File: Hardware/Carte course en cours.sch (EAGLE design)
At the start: 41 parts, among them J2 AVR_SPI_PROG_3X2NS, J3 PWR IN, J4 RC receiver, J5 ESC, J6 ESC, J7 MICRO-SD_CARD_SOCKET, J8 ESC, U1 LM317, U2 ATMEGA328P_TQFP, U3 FT232RL, U4 MPU6050, Y1 8MHz

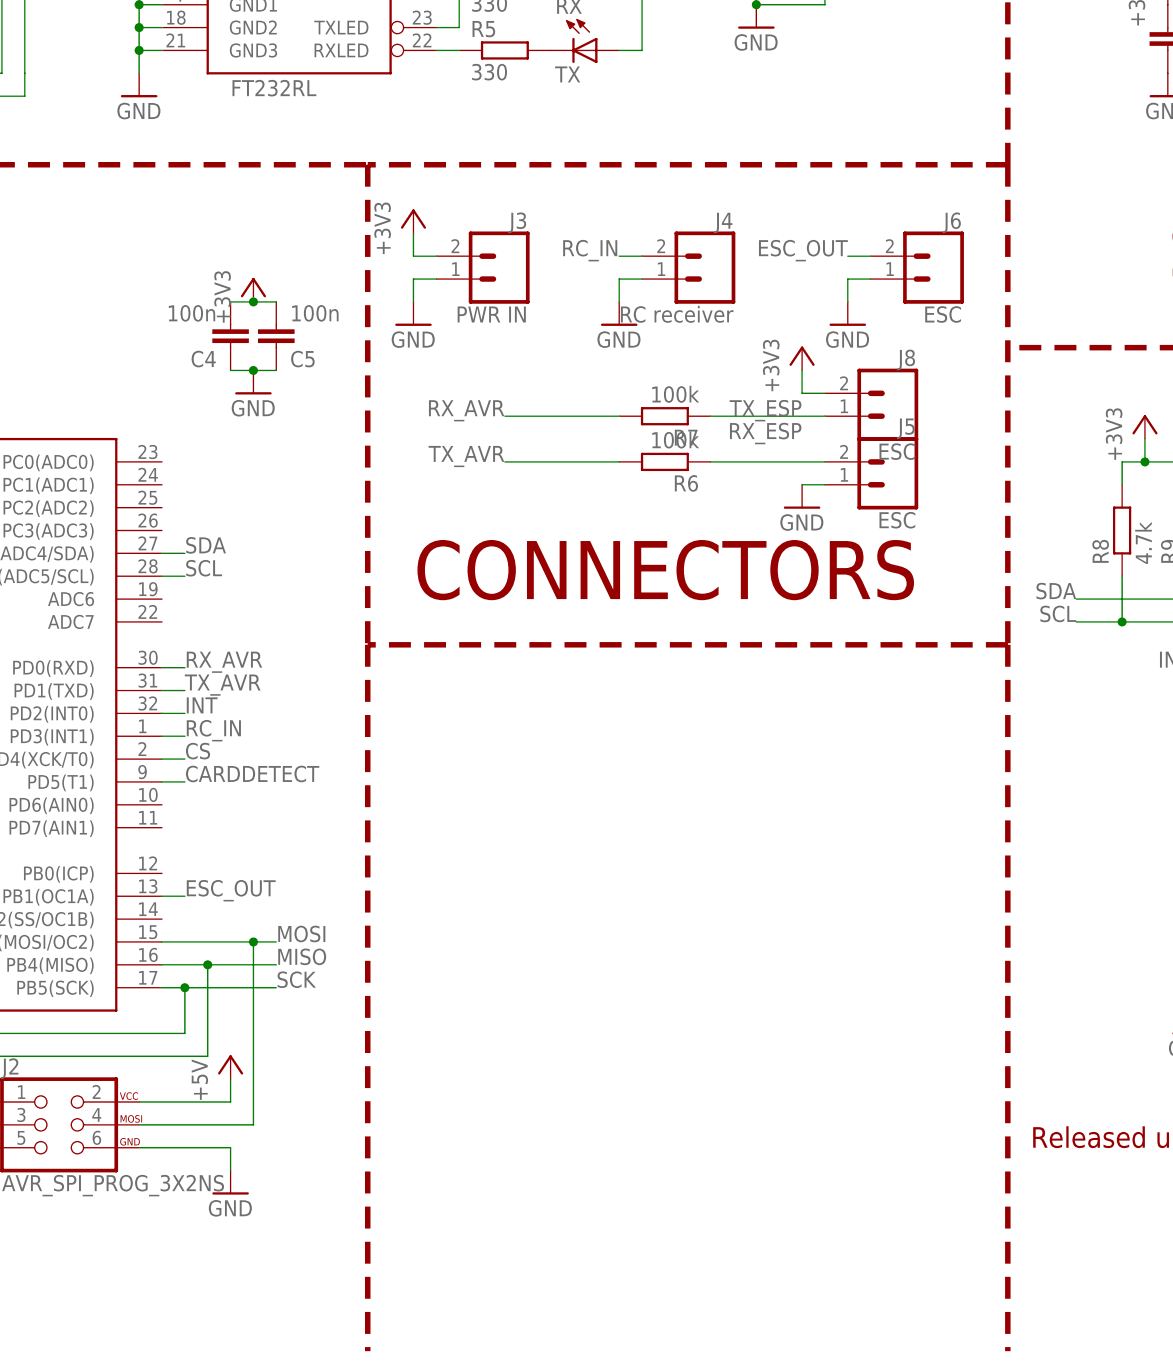
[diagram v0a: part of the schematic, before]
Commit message: Add 4 GPIO
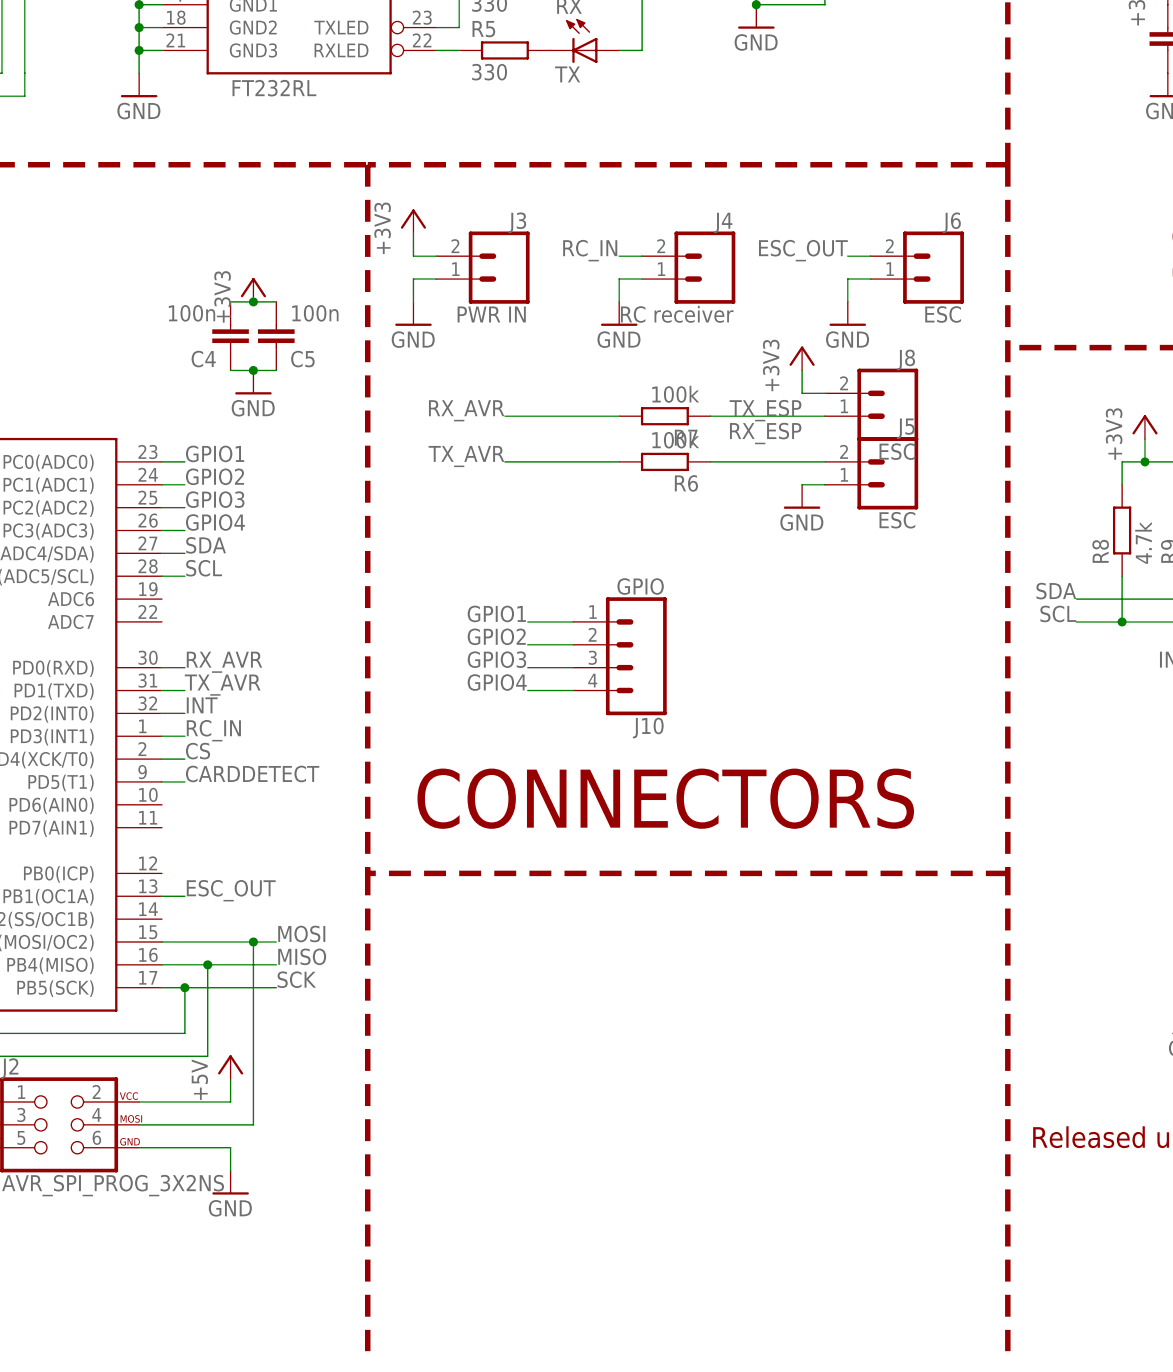
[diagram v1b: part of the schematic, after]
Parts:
- added J10: GPIO, SparkFun-Connectors:CONN_04
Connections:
- new net GPIO1: J10.1, U2.PC0(ADC0)
- new net GPIO2: J10.2, U2.PC1(ADC1)
- new net GPIO3: J10.3, U2.PC2(ADC2)
- new net GPIO4: J10.4, U2.PC3(ADC3)
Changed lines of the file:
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@@
 <?xml version="1.0" encoding="utf-8"?>
 <!DOCTYPE eagle SYSTEM "eagle.dtd">
-<eagle version="8.5.0">
+<eagle version="8.7.0">
 <drawing>
 <settings>
@@
 <part name="P+2" library="supply1" library_urn="urn:adsk.eagle:library:371" deviceset="+5V" device=""/>
 <part name="LOGO1" library="SparkFun-Aesthetics" library_urn="urn:adsk.eagle:library:507" deviceset="OSHW-LOGO" device="M" package3d_urn="urn:adsk.eagle:package:37126/1"/>
+<part name="J10" library="SparkFun-Connectors" library_urn="urn:adsk.eagle:library:513" deviceset="CONN_04" device="" package3d_urn="urn:adsk.eagle:package:38085/1" value="GPIO"/>
 </parts>
 <sheets>
@@
 <plain>
 <wire x1="272.796" y1="111.76" x2="167.64" y2="111.76" width="0.6096" layer="94" style="longdash"/>
-<wire x1="167.64" y1="132.08" x2="167.64" y2="78.74" width="0.6096" layer="94" style="longdash"/>
-<wire x1="167.64" y1="78.74" x2="167.64" y2="0.254" width="0.6096" layer="94" style="longdash"/>
+<wire x1="167.64" y1="132.08" x2="167.64" y2="53.34" width="0.6096" layer="94" style="longdash"/>
+<wire x1="167.64" y1="53.34" x2="167.64" y2="0.254" width="0.6096" layer="94" style="longdash"/>
 <wire x1="167.64" y1="132.08" x2="167.64" y2="178.816" width="0.6096" layer="94" style="longdash"/>
 <wire x1="0.254" y1="132.08" x2="96.52" y2="132.08" width="0.6096" layer="94" style="longdash"/>
-<wire x1="96.52" y1="132.08" x2="96.52" y2="78.74" width="0.6096" layer="94" style="longdash"/>
-<wire x1="96.52" y1="78.74" x2="96.52" y2="0.254" width="0.6096" layer="94" style="longdash"/>
+<wire x1="96.52" y1="132.08" x2="96.52" y2="53.34" width="0.6096" layer="94" style="longdash"/>
+<wire x1="96.52" y1="53.34" x2="96.52" y2="0.254" width="0.6096" layer="94" style="longdash"/>
 <wire x1="167.64" y1="132.08" x2="96.52" y2="132.08" width="0.6096" layer="94" style="longdash"/>
 <text x="10.16" y="15.24" size="6.4516" layer="94" font="vector" ratio="12">MCU</text>
@@
 <text x="116.84" y="162.56" size="6.4516" layer="94" font="vector" ratio="12">FTDI</text>
 <text x="170.18" y="22.86" size="2.286" layer="94" font="vector" ratio="12">Released under the GNU General Public License v3.0</text>
-<wire x1="167.64" y1="78.74" x2="96.52" y2="78.74" width="0.6096" layer="94" style="longdash"/>
-<text x="101.6" y="83.82" size="6.4516" layer="94" font="vector" ratio="12">CONNECTORS</text>
+<wire x1="167.64" y1="53.34" x2="96.52" y2="53.34" width="0.6096" layer="94" style="longdash"/>
+<text x="101.6" y="58.42" size="6.4516" layer="94" font="vector" ratio="12">CONNECTORS</text>
 </plain>
 <instances>
@@
 <instance part="P+2" gate="1" x="81.28" y="33.02"/>
 <instance part="LOGO1" gate="G$1" x="259.08" y="30.48"/>
+<instance part="J10" gate="G$1" x="124.46" y="78.74" rot="R180"/>
 </instances>
 <busses>
@@
 </segment>
 </net>
+<net name="GPIO1" class="0">
+<segment>
+<pinref part="U2" gate="U$1" pin="PC0(ADC0)"/>
+<wire x1="73.66" y1="99.06" x2="76.2" y2="99.06" width="0.1524" layer="91"/>
+<label x="76.2" y="99.06" size="1.778" layer="95"/>
+</segment>
+<segment>
+<pinref part="J10" gate="G$1" pin="1"/>
+<wire x1="119.38" y1="81.28" x2="114.3" y2="81.28" width="0.1524" layer="91"/>
+<label x="114.3" y="81.28" size="1.778" layer="95" rot="MR0"/>
+</segment>
+</net>
+<net name="GPIO2" class="0">
+<segment>
+<pinref part="U2" gate="U$1" pin="PC1(ADC1)"/>
+<wire x1="73.66" y1="96.52" x2="76.2" y2="96.52" width="0.1524" layer="91"/>
+<label x="76.2" y="96.52" size="1.778" layer="95"/>
+</segment>
+<segment>
+<pinref part="J10" gate="G$1" pin="2"/>
+<wire x1="119.38" y1="78.74" x2="114.3" y2="78.74" width="0.1524" layer="91"/>
+<label x="114.3" y="78.74" size="1.778" layer="95" rot="MR0"/>
+</segment>
+</net>
+<net name="GPIO3" class="0">
+<segment>
+<pinref part="U2" gate="U$1" pin="PC2(ADC2)"/>
+<wire x1="73.66" y1="93.98" x2="76.2" y2="93.98" width="0.1524" layer="91"/>
+<label x="76.2" y="93.98" size="1.778" layer="95"/>
+</segment>
+<segment>
+<pinref part="J10" gate="G$1" pin="3"/>
+<wire x1="119.38" y1="76.2" x2="114.3" y2="76.2" width="0.1524" layer="91"/>
+<label x="114.3" y="76.2" size="1.778" layer="95" rot="MR0"/>
+</segment>
+</net>
+<net name="GPIO4" class="0">
+<segment>
+<pinref part="U2" gate="U$1" pin="PC3(ADC3)"/>
+<wire x1="73.66" y1="91.44" x2="76.2" y2="91.44" width="0.1524" layer="91"/>
+<label x="76.2" y="91.44" size="1.778" layer="95"/>
+</segment>
+<segment>
+<pinref part="J10" gate="G$1" pin="4"/>
+<wire x1="119.38" y1="73.66" x2="114.3" y2="73.66" width="0.1524" layer="91"/>
+<label x="114.3" y="73.66" size="1.778" layer="95" rot="MR0"/>
+</segment>
+</net>
